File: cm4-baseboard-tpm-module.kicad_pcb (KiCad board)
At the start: 6 copper layers, 0 parts

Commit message: [#104798] Make full placement and layout, clear DRC
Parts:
- added C1: C_100n_25V_0402, antmicro-footprints:C_0402_1005Metric, F.Cu at (164.2, 124.9)
- added C2: C_100n_25V_0402, antmicro-footprints:C_0402_1005Metric, F.Cu at (161.0, 117.0)
- added C3: C_1u_10V_X7R_0402, antmicro-footprints:C_0402_1005Metric, F.Cu at (161.0, 115.9)
- added C4: C_100n_25V_0402, antmicro-footprints:C_0402_1005Metric, F.Cu at (166.8, 119.7)
- added C5: C_100n_25V_0402, antmicro-footprints:C_0402_1005Metric, F.Cu at (158.9, 123.2)
- added J1: Plug_Samtec_ERM5_2x20_ERM5-020-05.0-L-DV-K-TR, antmicro-footprints:Conn_Plug_Samtec_ERM5_2x20_ERM5-020-05.0-L-DV-K-TR, B.Cu at (174.9, 121.0)
- added N1001: antmicro_logo, antmicro-footprints:antmicro-logo_scaled_12mm, F.Cu at (164.6, 127.5)
- added R1: R_0R_0402, antmicro-footprints:R_0402_1005Metric, F.Cu at (168.9, 123.3)
- added R10: R_10k_0402, antmicro-footprints:R_0402_1005Metric, F.Cu at (168.9, 122.2)
- added R11: R_10k_0402, antmicro-footprints:R_0402_1005Metric, F.Cu at (162.1, 124.9)
- added R2: R_0R_0402, antmicro-footprints:R_0402_1005Metric, F.Cu at (168.9, 121.2)
- added R3: R_0R_0402, antmicro-footprints:R_0402_1005Metric, F.Cu at (168.9, 119.0)
- added R4: R_0R_0402, antmicro-footprints:R_0402_1005Metric, F.Cu at (168.9, 120.1)
- added R5: R_0R_0402, antmicro-footprints:R_0402_1005Metric, F.Cu at (168.9, 124.5)
- added R6: R_0R_0402, antmicro-footprints:R_0402_1005Metric, F.Cu at (168.9, 125.5)
- added R7: R_0R_0402, antmicro-footprints:R_0402_1005Metric, F.Cu at (168.9, 117.9)
- added R8: R_0R_0402, antmicro-footprints:R_0402_1005Metric, F.Cu at (168.9, 116.8)
- added R9: R_0R_0402, antmicro-footprints:R_0402_1005Metric, F.Cu at (168.9, 115.7)
- added U2: SLB9672XU20FW1624XTMA1, antmicro-footprints:QFN-32-1EP_5x5mm_P0.5mm, F.Cu at (162.9, 121.0)
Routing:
- net GND: track 0.00 -> 29.8 mm, vias 0 -> 12
- net /GPIO_02_R: track 0.00 -> 20.5 mm
- net /GPIO_01_R: track 0.00 -> 18.2 mm
- net /GPIO_00_R: track 0.00 -> 16.4 mm
- net +3V3: track 0.00 -> 13.7 mm, vias 0 -> 6
- net /SPI.SCLK: track 0.00 -> 9.67 mm, vias 0 -> 1
- net /SPI.MISO: track 0.00 -> 7.79 mm, vias 0 -> 1
- net /SPI.MOSI: track 0.00 -> 7.53 mm, vias 0 -> 1
- net /~{RST}_R: track 0.00 -> 4.88 mm
- net /~{RST}: track 0.00 -> 4.40 mm, vias 0 -> 1
- net /SPI.~{CS}: track 0.00 -> 4.25 mm, vias 0 -> 1
- net /SPI.~{CS}_R: track 0.00 -> 4.23 mm
- net /~{PIRQ}: track 0.00 -> 4.17 mm, vias 0 -> 1
- net /GPIO_00: track 0.00 -> 4.12 mm, vias 0 -> 1
- net /~{PIRQ}_R: track 0.00 -> 4.05 mm
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- added copper zone on B.Cu, net +3V3
- added copper zone on In1.Cu, net GND
- added copper zone on In2.Cu, net GND
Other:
- board outline added: 20 x 21 mm
- copper layers 6 -> 4
- board text added: "CM4 Baseboard TPM Module"
- board text added: "Rev. ${REVISION} 09/2026"
- board text removed: "Change stackup to 4 layers (recalculate impedance controlled traces)! Add stackup table next to the board!"

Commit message: [#104798] Add measurements, bump date
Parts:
- moved R6 202.1 mm to (339.2, 234.4)
- moved C2 202.1 mm to (331.3, 225.8)
- moved C3 202.1 mm to (331.3, 224.8)
- moved C4 202.1 mm to (337.1, 228.5)
- moved N1001 202.1 mm to (334.8, 236.3)
- moved R10 202.1 mm to (339.2, 231.1)
- moved R11 202.1 mm to (332.4, 233.8)
- moved R2 202.1 mm to (339.2, 230.1)
- moved R3 202.1 mm to (339.2, 227.8)
- moved R4 202.1 mm to (339.2, 228.9)
- moved R7 202.1 mm to (339.2, 226.8)
- moved R8 202.1 mm to (339.2, 225.7)
- moved R9 202.1 mm to (339.2, 224.6)
- moved C1 202.1 mm to (334.4, 233.8)
- moved C5 202.1 mm to (329.2, 232.0)
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
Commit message: [#104798] Clear DRC
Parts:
- added D1: LED_G_0603_KP-1608CGCK, antmicro-footprints:LED_0603_1608Metric_G, F.Cu at (336.0, 221.2)
- added FD1: Fiducial_1mm_Mask2mm, antmicro-footprints:Fiducial_1mm_Mask2mm, F.Cu at (334.1, 218.0)
- added FD2: Fiducial_1mm_Mask2mm, antmicro-footprints:Fiducial_1mm_Mask2mm, F.Cu at (334.0, 242.0)
- added MP1: MP_NPTH_Drill3.2mm, antmicro-footprints:MP_NPTH_Drill3.2mm, F.Cu at (330.5, 218.0)
- added MP2: MP_NPTH_Drill3.2mm, antmicro-footprints:MP_NPTH_Drill3.2mm, F.Cu at (330.5, 242.0)
- added N2: oshw_logo, antmicro-footprints:oshw-logo, F.Cu at (341.5, 219.9)
- added R12: R_470R_0402, antmicro-footprints:R_0402_1005Metric, F.Cu at (333.4, 221.2)
- added TP1: TP_Pad0.75mm_Drill0.2mm, antmicro-footprints:TP_Pad0.75mm_Drill0.2mm, F.Cu at (336.3, 242.1)
- added TP2: TP_Pad0.75mm_Drill0.2mm, antmicro-footprints:TP_Pad0.75mm_Drill0.2mm, F.Cu at (331.7, 221.2)
- moved N1 0.50 mm to (334.8, 236.8)
- renumbered C5 to C1, C1 to C2, C2 to C3, C3 to C5, N1001 to N1, U2 to U1
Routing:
- net Net-(D1-A): track 0.00 -> 1.42 mm
- net +3V3: track 13.7 -> 14.9 mm
- net GND: track 30.0 -> 31.0 mm, vias 12 -> 13
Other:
- board size 20 x 21 mm -> 20 x 29 mm

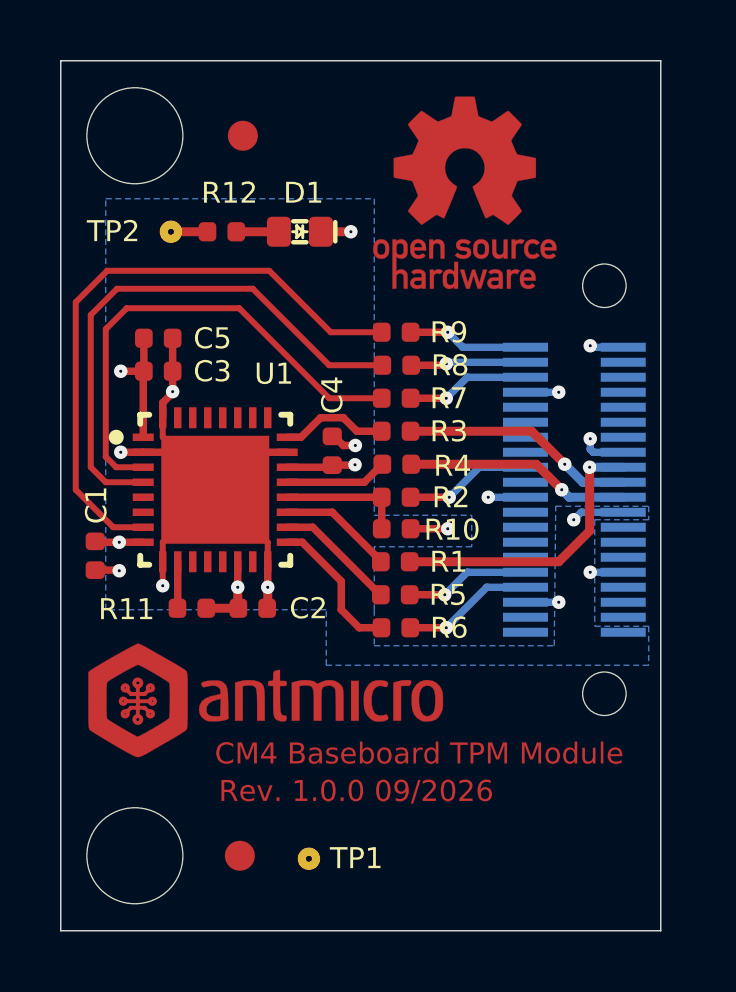
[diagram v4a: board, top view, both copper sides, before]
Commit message: [#104798] Add testpoints and reroute the PCB
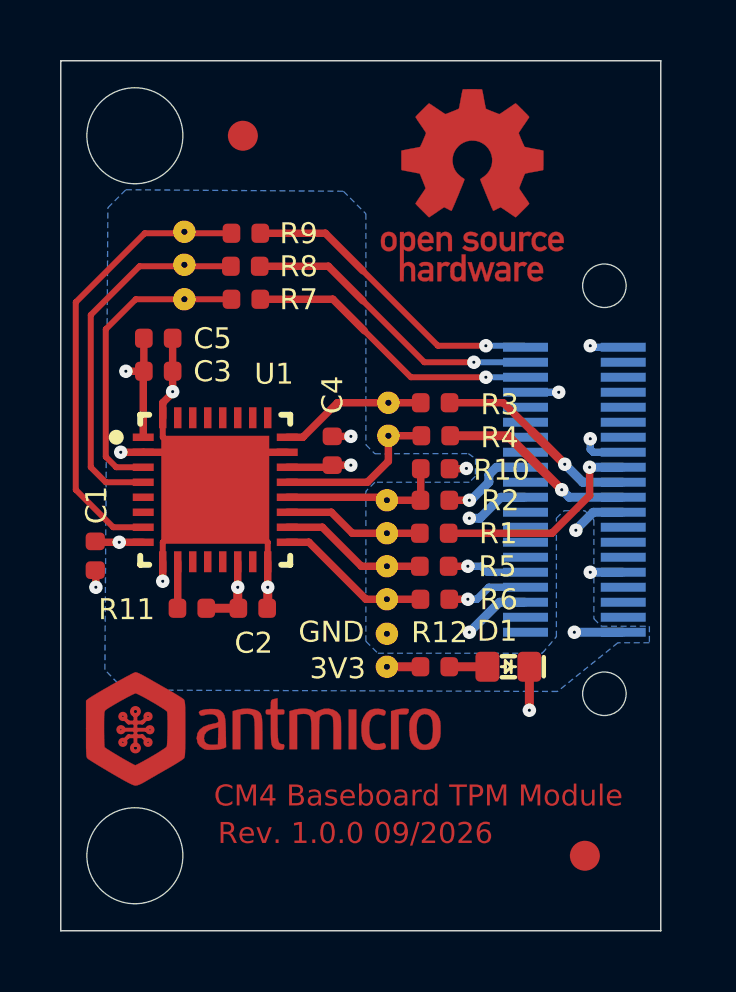
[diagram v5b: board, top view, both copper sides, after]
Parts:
- added TP10: TP_Pad0.75mm_Drill0.2mm, antmicro-footprints:TP_Pad0.75mm_Drill0.2mm, F.Cu at (332.1, 222.3)
- added TP11: TP_Pad0.75mm_Drill0.2mm, antmicro-footprints:TP_Pad0.75mm_Drill0.2mm, F.Cu at (332.1, 221.2)
- added TP3: TP_Pad0.75mm_Drill0.2mm, antmicro-footprints:TP_Pad0.75mm_Drill0.2mm, F.Cu at (338.9, 231.2)
- added TP4: TP_Pad0.75mm_Drill0.2mm, antmicro-footprints:TP_Pad0.75mm_Drill0.2mm, F.Cu at (338.9, 230.2)
- added TP5: TP_Pad0.75mm_Drill0.2mm, antmicro-footprints:TP_Pad0.75mm_Drill0.2mm, F.Cu at (338.9, 226.9)
- added TP6: TP_Pad0.75mm_Drill0.2mm, antmicro-footprints:TP_Pad0.75mm_Drill0.2mm, F.Cu at (338.9, 228.0)
- added TP7: TP_Pad0.75mm_Drill0.2mm, antmicro-footprints:TP_Pad0.75mm_Drill0.2mm, F.Cu at (338.9, 232.3)
- added TP8: TP_Pad0.75mm_Drill0.2mm, antmicro-footprints:TP_Pad0.75mm_Drill0.2mm, F.Cu at (338.9, 233.4)
- added TP9: TP_Pad0.75mm_Drill0.2mm, antmicro-footprints:TP_Pad0.75mm_Drill0.2mm, F.Cu at (332.1, 223.4)
- moved 3V3 16.2 mm to (338.9, 235.7), turned to 180 degrees
- moved R12 16.1 mm to (340.5, 235.7)
- moved D1 16.1 mm to (342.9, 235.7)
- moved FD2 11.5 mm to (345.5, 242.0)
- moved GND 7.94 mm to (338.9, 234.6)
- moved R8 6.03 mm to (334.2, 222.3)
- moved R7 6.00 mm to (334.2, 223.4)
- moved R9 6.00 mm to (334.2, 221.2)
- moved R10 2.39 mm to (340.5, 229.1)
- moved R5 1.61 mm to (340.5, 232.3)
- moved R6 1.61 mm to (340.5, 233.4)
- moved R1 1.61 mm to (340.5, 231.2)
- moved R3 1.61 mm to (340.5, 226.9)
- moved R4 1.61 mm to (340.5, 228.0)
- moved R2 1.29 mm to (340.5, 230.2)
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- renumbered TP2 to 3V3, TP1 to GND
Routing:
- net /GPIO_02: track 4.04 -> 10.4 mm
- net /GPIO_01: track 3.92 -> 10.2 mm
- net /GPIO_00_R: track 16.4 -> 10.3 mm
- net /GPIO_00: track 4.12 -> 9.92 mm
- net /GPIO_01_R: track 18.2 -> 12.4 mm
- net /GPIO_02_R: track 20.5 -> 15.2 mm
- net /SPI.SCLK: track 9.67 -> 7.28 mm
- net /SPI.MOSI_R: track 3.42 -> 5.61 mm
- net GND: track 31.0 -> 32.9 mm
- net /~{RST}: track 4.40 -> 2.71 mm
- net /~{PIRQ}: track 4.17 -> 2.64 mm
- net /SPI.~{CS}_R: track 4.23 -> 5.56 mm
- net /SPI.MISO_R: track 3.61 -> 4.93 mm
- net /SPI.~{CS}: track 4.25 -> 3.14 mm
- net /SPI.SCLK_R: track 3.82 -> 4.74 mm
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
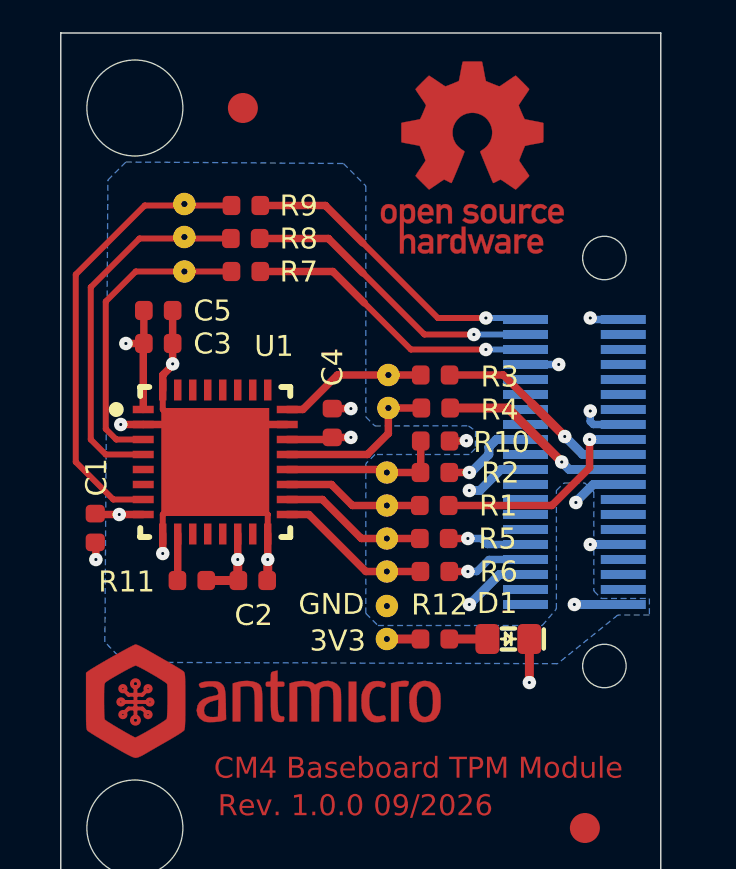
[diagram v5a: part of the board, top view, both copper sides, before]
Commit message: [#104798] Change SLB9672 3D model
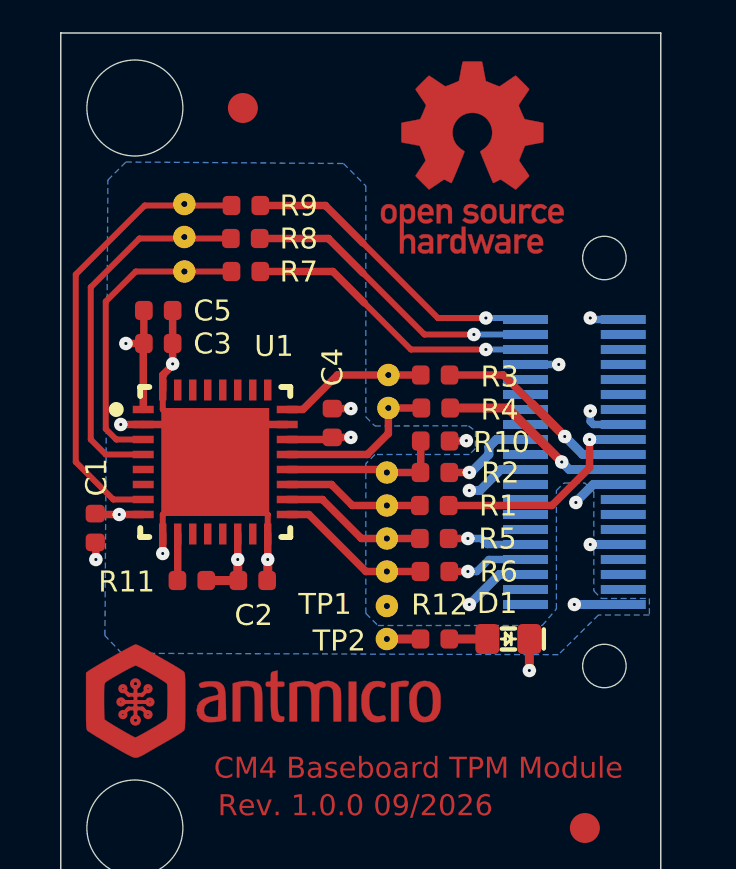
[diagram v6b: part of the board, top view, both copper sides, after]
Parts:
- renumbered GND to TP1, 3V3 to TP2
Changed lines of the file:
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@@
 		)
 		(embedded_fonts no)
-		(model "${KICAD10_3DMODEL_DIR}/FCQFN-32-1EP_5x5mm_P0.5mm.step"
+		(model "${KICAD10_3DMODEL_DIR}/HVQFN-32-1EP_5x5mm_P0.5mm_EP3.6x3.6mm.step"
 			(offset
 				(xyz 0 0 0)
@@
 		(layer "F.Cu")
 		(at 338.9 234.6)
-		(property "Reference" "GND"
+		(property "Reference" "TP1"
 			(at -2.95 0.35 0)
 			(layer "F.SilkS" knockout)
@@
 		(layer "F.Cu")
 		(at 338.9 235.7 180)
-		(property "Reference" "3V3"
+		(property "Reference" "TP2"
 			(at 0.7 0.35 0)
 			(layer "F.SilkS" knockout)
@@
 	)
 	(segment
-		(start 343.65 237.15)
-		(end 343.65 235.7)
-		(width 0.3)
-		(layer "F.Cu")
-		(net "GND")
-	)
-	(segment
 		(start 331.429 226.9)
 		(end 331.429 227.4)
@@
 		(net "GND")
 	)
+	(segment
+		(start 343.65 236.75)
+		(end 343.65 235.7)
+		(width 0.3)
+		(layer "F.Cu")
+		(net "GND")
+	)
 	(via
 		(at 344.629 226.55)
@@
 	)
 	(via
-		(at 343.65 237.15)
+		(at 343.65 236.75)
 		(size 0.45)
 		(drill 0.1)
@@
 	)
 	(segment
+		(start 341.08 235.7)
+		(end 342.25 235.7)
+		(width 0.3)
+		(layer "F.Cu")
+		(net "Net-(D1-A)")
+	)
+	(segment
 		(start 340.6 225)
 		(end 342.2 225)
@@
 	)
 	(segment
-		(start 341.08 235.7)
-		(end 342.25 235.7)
-		(width 0.3)
-		(layer "F.Cu")
-		(net "Net-(D1-A)")
-	)
-	(segment
 		(start 340.979 233.45)
 		(end 341.6 233.45)
@@
 				(xy 338.2 234.85) (xy 338.6 235.25) (xy 344.078571 235.25) (xy 344.55 234.7) (xy 344.55 230.75)
 				(xy 344.8 230.5) (xy 345.5 230.5) (xy 345.8 230.8) (xy 345.8 234.1) (xy 346.05 234.35) (xy 347.65 234.35)
-				(xy 347.65 234.9) (xy 346.6 234.9) (xy 344.589414 236.523935) (xy 330.15 236.476826) (xy 329.5 235.8)
+				(xy 347.65 234.9) (xy 345.95 234.9) (xy 344.61609 236.223543) (xy 330.065124 236.176069) (xy 329.50137 235.589046)
 				(xy 329.6 220.4) (xy 330.2 219.8)
 			)

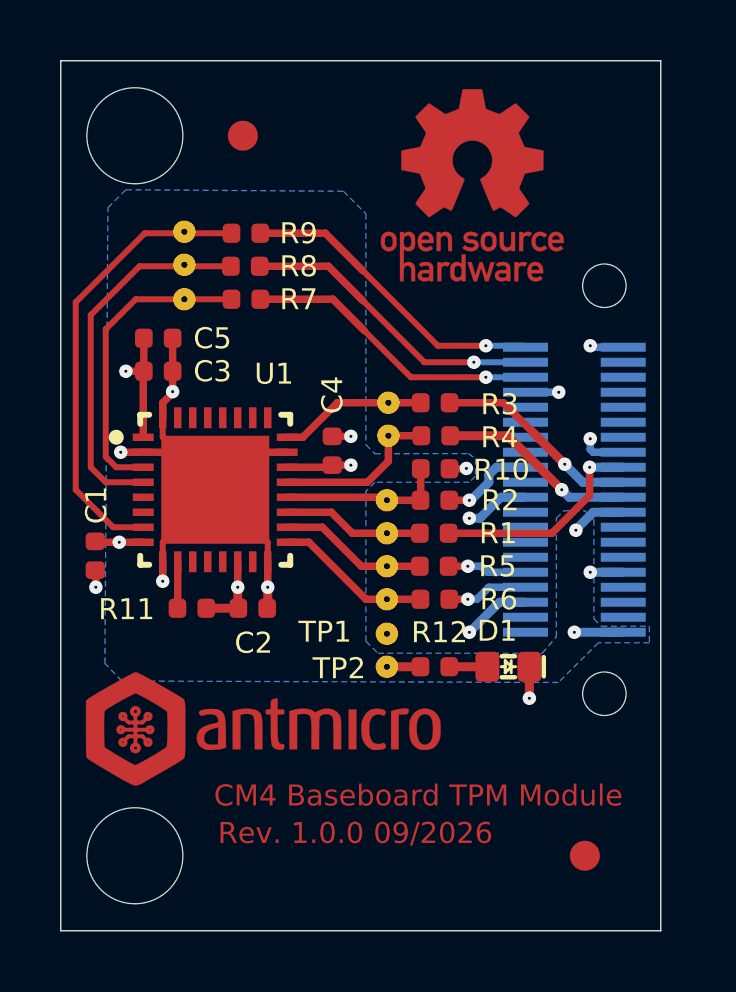
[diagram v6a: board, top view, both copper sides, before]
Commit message: [#104798] Create 2-layer board version
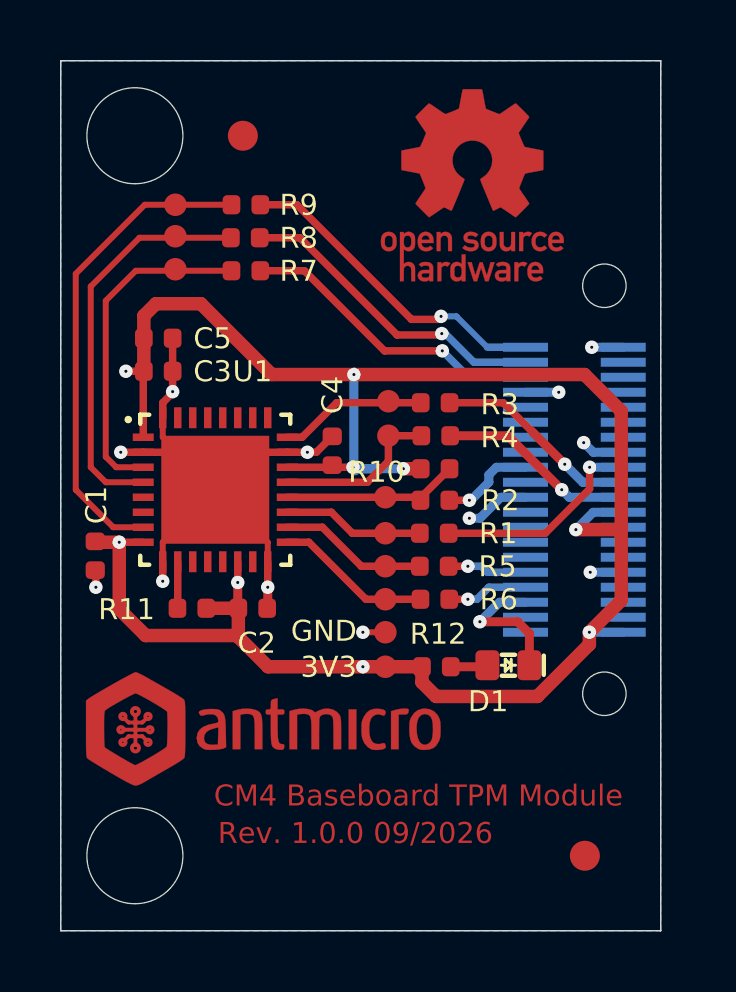
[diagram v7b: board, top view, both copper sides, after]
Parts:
- TP1, TP10, TP11, TP2, TP3, TP4, TP5, TP6, TP7, TP8, TP9: value TP_Pad0.75mm_Drill0.2mm -> TP_0.75mm_SMD; footprint antmicro-footprints:TP_Pad0.75mm_Drill0.2mm -> antmicro-footprints:TP_SMD_0.75mm
- U1: footprint antmicro-footprints:QFN-32-1EP_5x5mm_P0.5mm -> antmicro-footprints:UQFN-32-1EP_5x5mm_P0.5mm_EP3.6x3.6mm
- moved TP11 16.0 mm to (338.9, 235.7)
- moved TP8 13.1 mm to (331.9, 222.4)
- moved TP2 4.45 mm to (338.9, 231.2), turned to 0 degrees
- moved TP6 4.35 mm to (338.9, 232.3)
- moved TP4 3.30 mm to (338.9, 226.8)
- moved TP9 2.12 mm to (331.9, 221.3)
- moved TP10 2.02 mm to (331.9, 220.3)
- moved TP3 1.20 mm to (338.9, 230.1)
- moved TP7 1.10 mm to (338.9, 233.4)
- moved TP5 1.10 mm to (338.9, 228.0)
- moved R7 0.95 mm to (334.2, 222.5)
- moved R8 0.95 mm to (334.2, 221.4)
- moved R9 0.95 mm to (334.2, 220.3)
- moved TP1 0.07 mm to (338.9, 234.6)
- moved R12 0.05 mm to (340.6, 235.7)
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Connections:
- net /GPIO_00 renamed /GPIO_0
- net /GPIO_01 renamed /GPIO_1
- net /GPIO_02 renamed /GPIO_2
- R7 pad 2: /GPIO_00_R -> /GPIO_0_R
- R8 pad 2: /GPIO_01_R -> /GPIO_1_R
- R9 pad 2: /GPIO_02_R -> /GPIO_2_R
- TP10 pad 1: /GPIO_01_R -> /GPIO_2_R
- TP11 pad 1: /GPIO_02_R -> +3V3
- TP2 pad 1: +3V3 -> /SPI.SCLK_R
- TP3 pad 1: /SPI.SCLK_R -> /SPI.~{CS}_R
- TP4 pad 1: /SPI.~{CS}_R -> /SPI.MISO_R
- TP5 pad 1: /SPI.MISO_R -> /SPI.MOSI_R
- TP6 pad 1: /SPI.MOSI_R -> /~{PIRQ}_R
- TP7 pad 1: /~{PIRQ}_R -> /~{RST}_R
- TP8 pad 1: /~{RST}_R -> /GPIO_0_R
- TP9 pad 1: /GPIO_00_R -> /GPIO_1_R
- U1 pad 3: /GPIO_00_R -> /GPIO_0_R
- U1 pad 4: /GPIO_01_R -> /GPIO_1_R
- U1 pad 7: /GPIO_02_R -> /GPIO_2_R
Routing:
- net +3V3: track 15.4 -> 69.8 mm, vias 7 -> 9
- net /GPIO_2_R: track 0.00 -> 16.1 mm
- net /GPIO_02_R: track 15.2 -> 0.00 mm
- net /GPIO_1_R: track 0.00 -> 13.3 mm
- net /GPIO_01_R: track 12.4 -> 0.00 mm
- net /GPIO_0_R: track 0.00 -> 11.2 mm
- net /GPIO_00_R: track 10.3 -> 0.00 mm
- net GND: track 32.5 -> 35.6 mm
- added copper zone on B.Cu, net GND
- removed copper zone on B.Cu, net +3V3
- removed copper zone on In1.Cu, net GND
- removed copper zone on In2.Cu, net GND
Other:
- copper layers 4 -> 2
- board text added: "3V3"
- board text added: "GND"
